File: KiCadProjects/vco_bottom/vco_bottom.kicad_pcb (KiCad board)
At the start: 2 copper layers, 160 x 100 mm, 93 parts, among them J1 Conn_02x08_Odd_Even, J2 Conn_02x08_Odd_Even, J3 Conn_01x03_Pin, J4 Conn_01x03_Pin, J5 Conn_01x03_Pin, J6 Conn_02x08_Odd_Even, Q1 BC558, Q2 BC548, Q3 BC558, Q4 BC548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

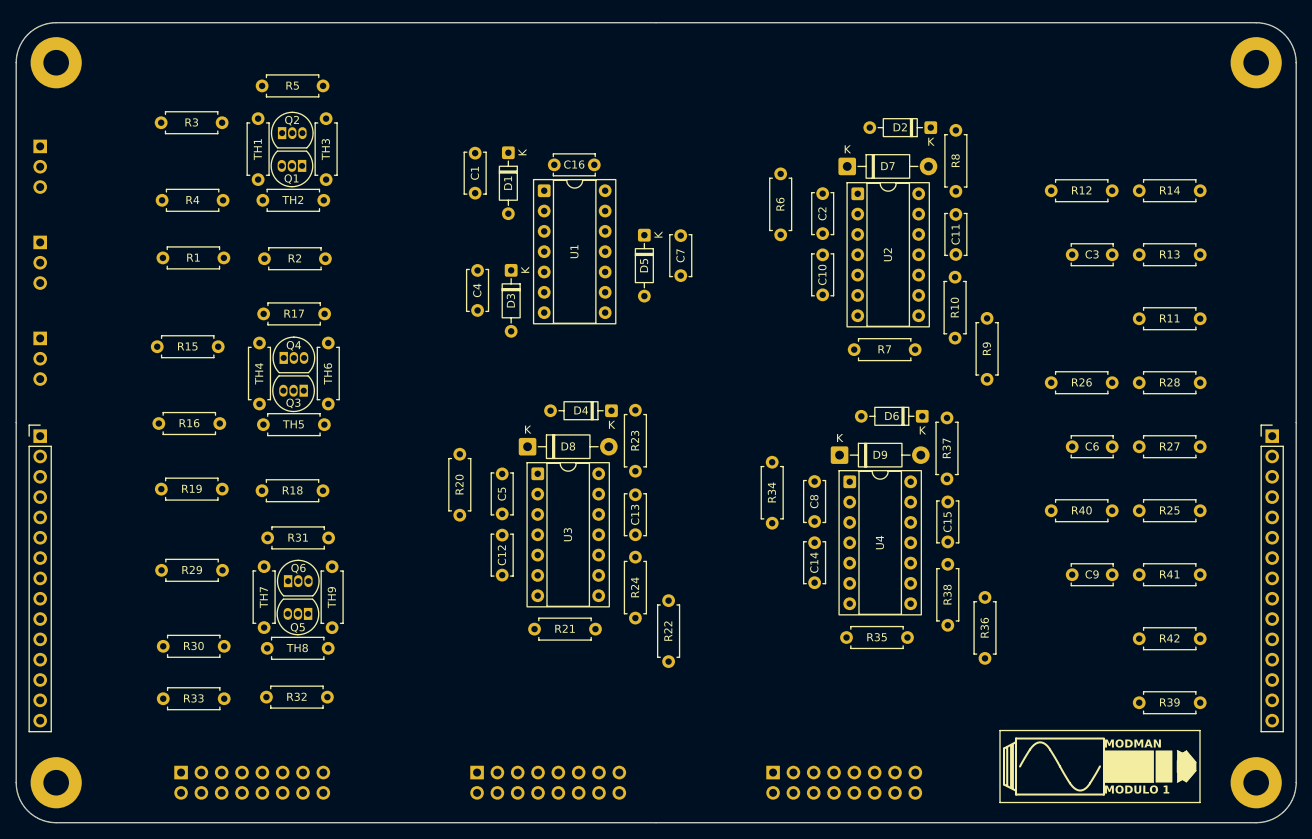
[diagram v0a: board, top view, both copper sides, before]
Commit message: added vco top and bottom
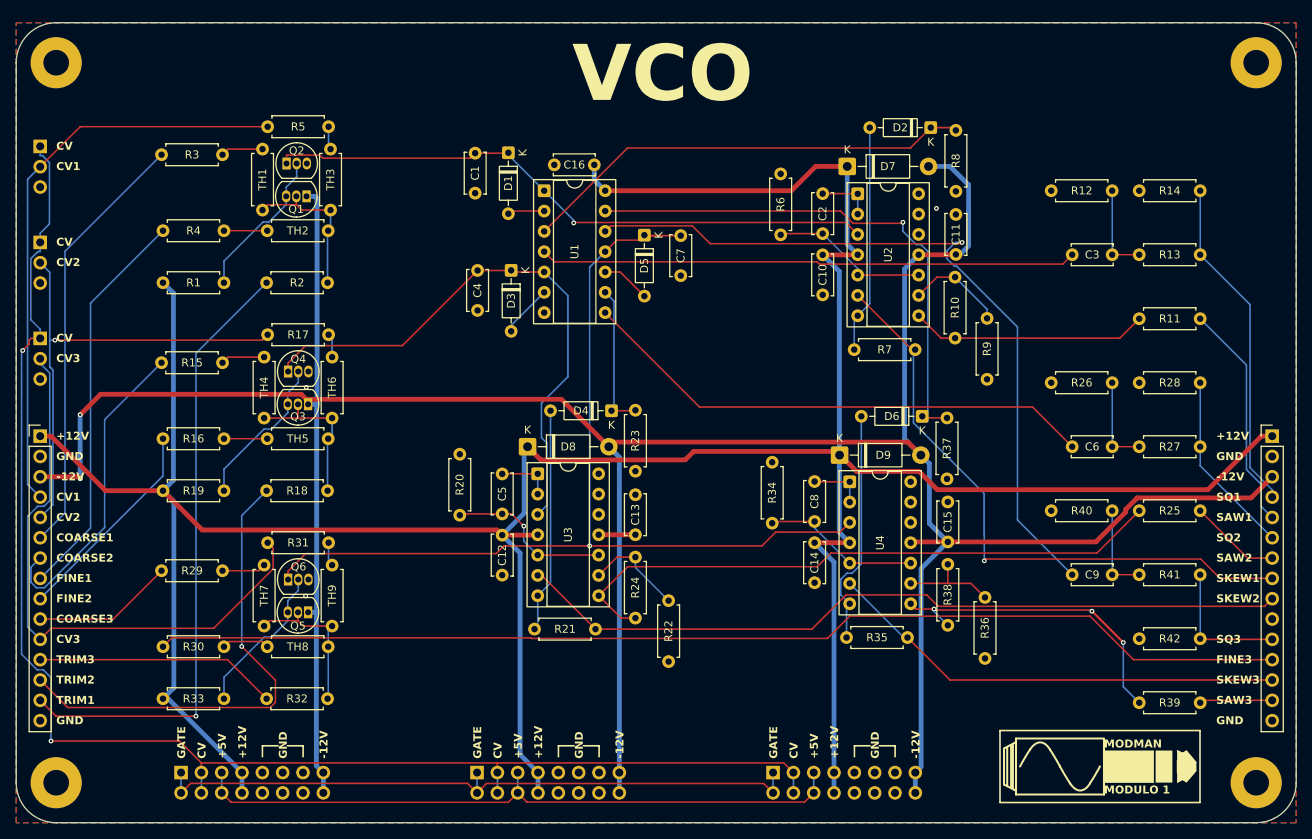
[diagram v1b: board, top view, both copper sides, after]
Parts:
- moved R18 8.19 mm to (108.9, 88.5), turned to 180 degrees
- moved R32 7.64 mm to (108.9, 114.5), turned to 180 degrees
- moved R5 5.15 mm to (101.4, 43.0)
- moved R3 4.00 mm to (95.8, 46.5)
- moved TH1 3.85 mm to (100.8, 45.8)
- moved TH3 3.85 mm to (109.3, 45.8)
- moved Q1 3.84 mm to (106.3, 51.7)
- moved Q2 3.84 mm to (103.8, 47.6)
- moved TH2 3.84 mm to (101.4, 56.0)
- moved R4 3.80 mm to (88.3, 56.0)
- moved R1 3.10 mm to (88.3, 62.5)
- moved R2 3.01 mm to (108.9, 62.5)
- moved R17 2.65 mm to (101.4, 69.0)
- moved R15 2.07 mm to (95.8, 72.5)
- moved R16 1.97 mm to (88.3, 82.0)
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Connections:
- C1 pad 2: -12V -> GND
- C10 pad 2: -12V -> GND
- C11 pad 1: -12V -> GND
- C12 pad 2: -12V -> GND
- C13 pad 1: -12V -> GND
- C14 pad 2: -12V -> GND
- C15 pad 1: -12V -> GND
- C16 pad 2: -12V -> GND
- C4 pad 2: -12V -> GND
- C7 pad 2: -12V -> GND
- J1 pad 10: -12V -> GND
- J1 pad 11: -12V -> GND
- J1 pad 12: -12V -> GND
- J1 pad 13: -12V -> GND
- J1 pad 14: -12V -> GND
- J1 pad 9: -12V -> GND
- J2 pad 10: unconnected-(J2-Pin_10-Pad10) -> GND
- J2 pad 11: unconnected-(J2-Pin_11-Pad11) -> GND
- J2 pad 12: unconnected-(J2-Pin_12-Pad12) -> GND
- J2 pad 13: unconnected-(J2-Pin_13-Pad13) -> GND
- J2 pad 14: unconnected-(J2-Pin_14-Pad14) -> GND
- J2 pad 15: unconnected-(J2-Pin_15-Pad15) -> -12V
- J2 pad 16: unconnected-(J2-Pin_16-Pad16) -> -12V
- J2 pad 5: unconnected-(J2-Pin_5-Pad5) -> +5V
- J2 pad 6: unconnected-(J2-Pin_6-Pad6) -> +5V
- J2 pad 7: unconnected-(J2-Pin_7-Pad7) -> +12V
- J2 pad 8: unconnected-(J2-Pin_8-Pad8) -> +12V
- J2 pad 9: unconnected-(J2-Pin_9-Pad9) -> GND
- J6 pad 10: unconnected-(J6-Pin_10-Pad10) -> GND
- J6 pad 11: unconnected-(J6-Pin_11-Pad11) -> GND
- J6 pad 12: unconnected-(J6-Pin_12-Pad12) -> GND
- J6 pad 13: unconnected-(J6-Pin_13-Pad13) -> GND
- J6 pad 14: unconnected-(J6-Pin_14-Pad14) -> GND
- J6 pad 15: unconnected-(J6-Pin_15-Pad15) -> -12V
- J6 pad 16: unconnected-(J6-Pin_16-Pad16) -> -12V
- J6 pad 5: unconnected-(J6-Pin_5-Pad5) -> +5V
- J6 pad 6: unconnected-(J6-Pin_6-Pad6) -> +5V
- J6 pad 7: unconnected-(J6-Pin_7-Pad7) -> +12V
- J6 pad 8: unconnected-(J6-Pin_8-Pad8) -> +12V
- J6 pad 9: unconnected-(J6-Pin_9-Pad9) -> GND
- Q2 pad 3: -12V -> GND
- Q4 pad 3: -12V -> GND
- Q6 pad 3: -12V -> GND
- R12 pad 2: -12V -> GND
- R14 pad 2: -12V -> GND
- R20 pad 2: -12V -> GND
- R22 pad 2: -12V -> GND
- R23 pad 2: -12V -> GND
- R26 pad 2: -12V -> GND
- R28 pad 2: -12V -> GND
- R34 pad 2: -12V -> GND
- R36 pad 2: -12V -> GND
- R37 pad 2: -12V -> GND
- R40 pad 2: -12V -> GND
- R42 pad 2: -12V -> GND
- R6 pad 2: -12V -> GND
- R8 pad 2: -12V -> GND
- R9 pad 2: -12V -> GND
- T1 pad 0: -12V -> GND
- T1 pad 15: -12V -> GND
- T1 pad 17: -12V -> GND
- T1 pad 2: -12V -> GND
- T1 pad 30: -12V -> GND
- U1 pad 7: -12V -> GND
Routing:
- net +12V: track 0.00 -> 408.4 mm
- net -12V: track 0.00 -> 393.6 mm, vias 0 -> 2
- net CV: track 0.00 -> 184.7 mm, vias 0 -> 2
- net FINE3: track 0.00 -> 142.5 mm
- net Net-(D5-K): track 0.00 -> 124.0 mm, vias 0 -> 1
- net SKEW2: track 0.00 -> 97.3 mm
- net Net-(C9-Pad1): track 0.00 -> 95.4 mm, vias 0 -> 1
- net GATE: track 0.00 -> 83.6 mm
- net +5V: track 0.00 -> 83.5 mm
- net TRIM1: track 0.00 -> 78.1 mm, vias 0 -> 1
- net Net-(D1-K): track 0.00 -> 77.8 mm, vias 0 -> 1
- net Net-(R24-Pad2): track 0.00 -> 77.7 mm
- net SKEW1: track 0.00 -> 77.2 mm, vias 0 -> 1
- net CV3: track 0.00 -> 74.1 mm
- net CV1: track 0.00 -> 73.1 mm
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- added copper zone on B.Cu, net GND
- added copper zone on F.Cu, net GND
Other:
- board text added: "+12V"
- board text added: "+5V"
- board text added: "-12V"
- board text added: "COARSE1"
- board text added: "COARSE2"
- board text added: "COARSE3"
- board text added: "CV"
- board text added: "CV1"
- board text added: "CV2"
- board text added: "CV3"
- board text added: "FINE1"
- board text added: "FINE2"
- board text added: "FINE3"
- board text added: "GATE"
- board text added: "GND"
- board text added: "SAW1"
- board text added: "SAW2"
- board text added: "SAW3"
- board text added: "SKEW1"
- board text added: "SKEW2"
- board text added: "SKEW3"
- board text added: "SQ1"
- board text added: "SQ2"
- board text added: "SQ3"
- board text added: "TRIM1"
- board text added: "TRIM2"
- board text added: "TRIM3"
- board text added: "VCO"
